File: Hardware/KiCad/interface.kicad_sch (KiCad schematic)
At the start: 26 parts, among them J6 UART, J7 OLED, SW10 SW_Push_45deg, SW11 SW_Push_45deg, SW12 SW_Push_45deg, SW13 SW_Push_45deg, SW14 SW_Push_45deg, SW15 SW_Push_45deg, SW16 SW_Push_45deg, SW17 SW_Push_45deg, SW2 SW_Push_45deg, SW3 SW_Push_45deg, SW4 SW_Push_45deg, SW5 SW_Push_45deg, SW6 SW_Push_45deg, SW7 SW_Push_45deg, SW8 SW_Push_45deg, SW9 SW_Push_45deg

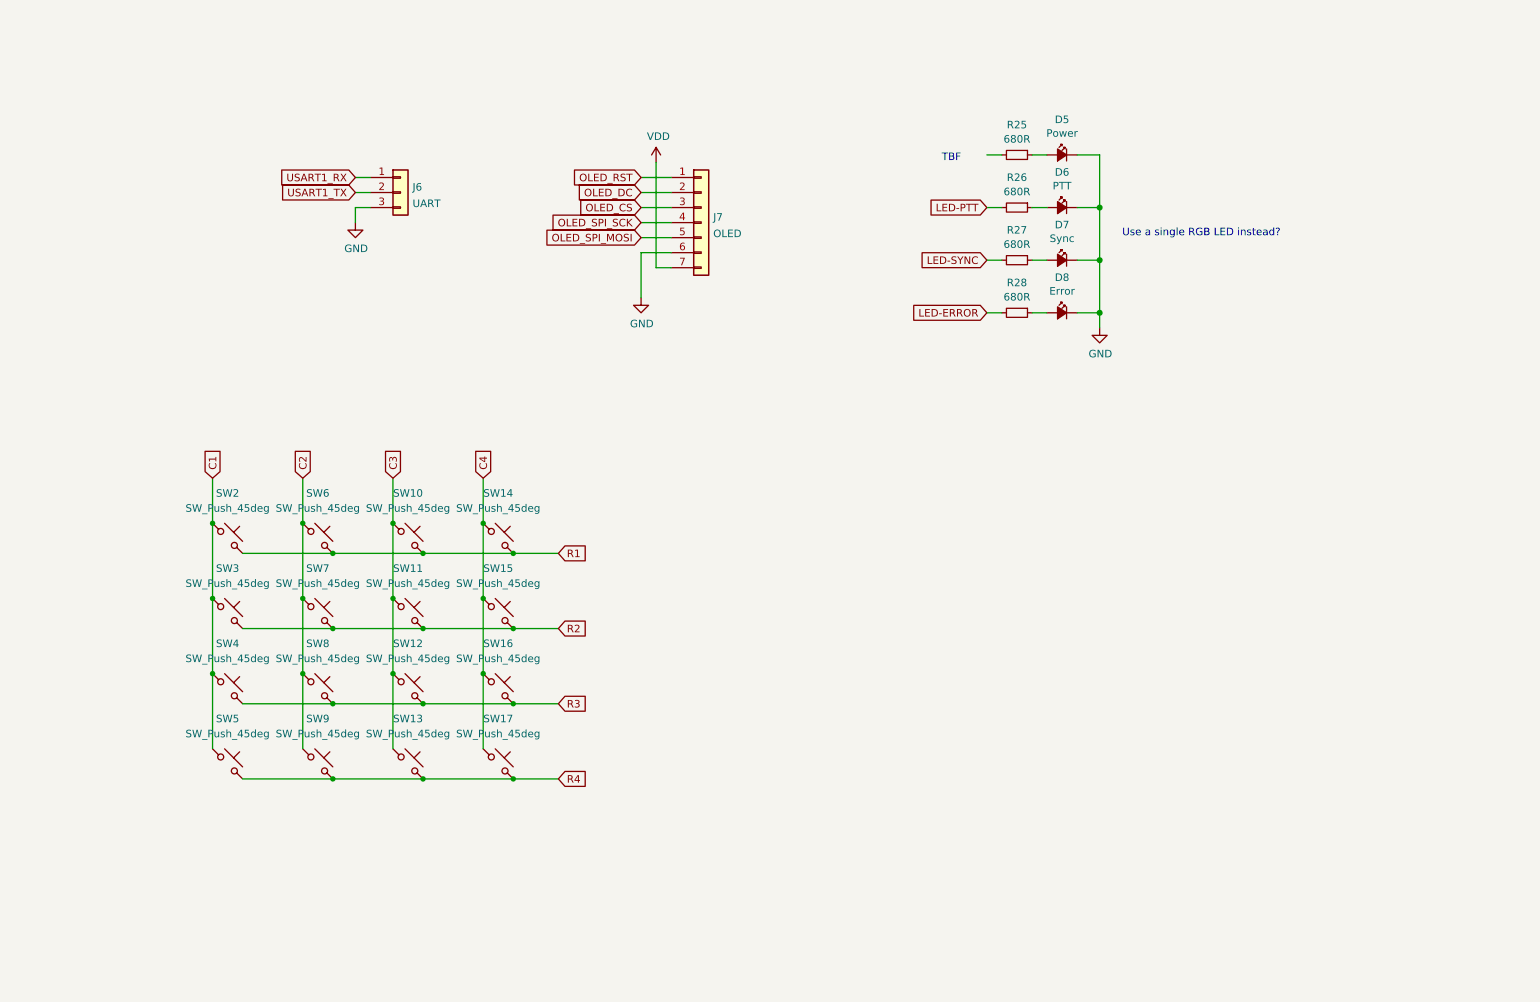
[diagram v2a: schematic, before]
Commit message: Connected SD card to the micro
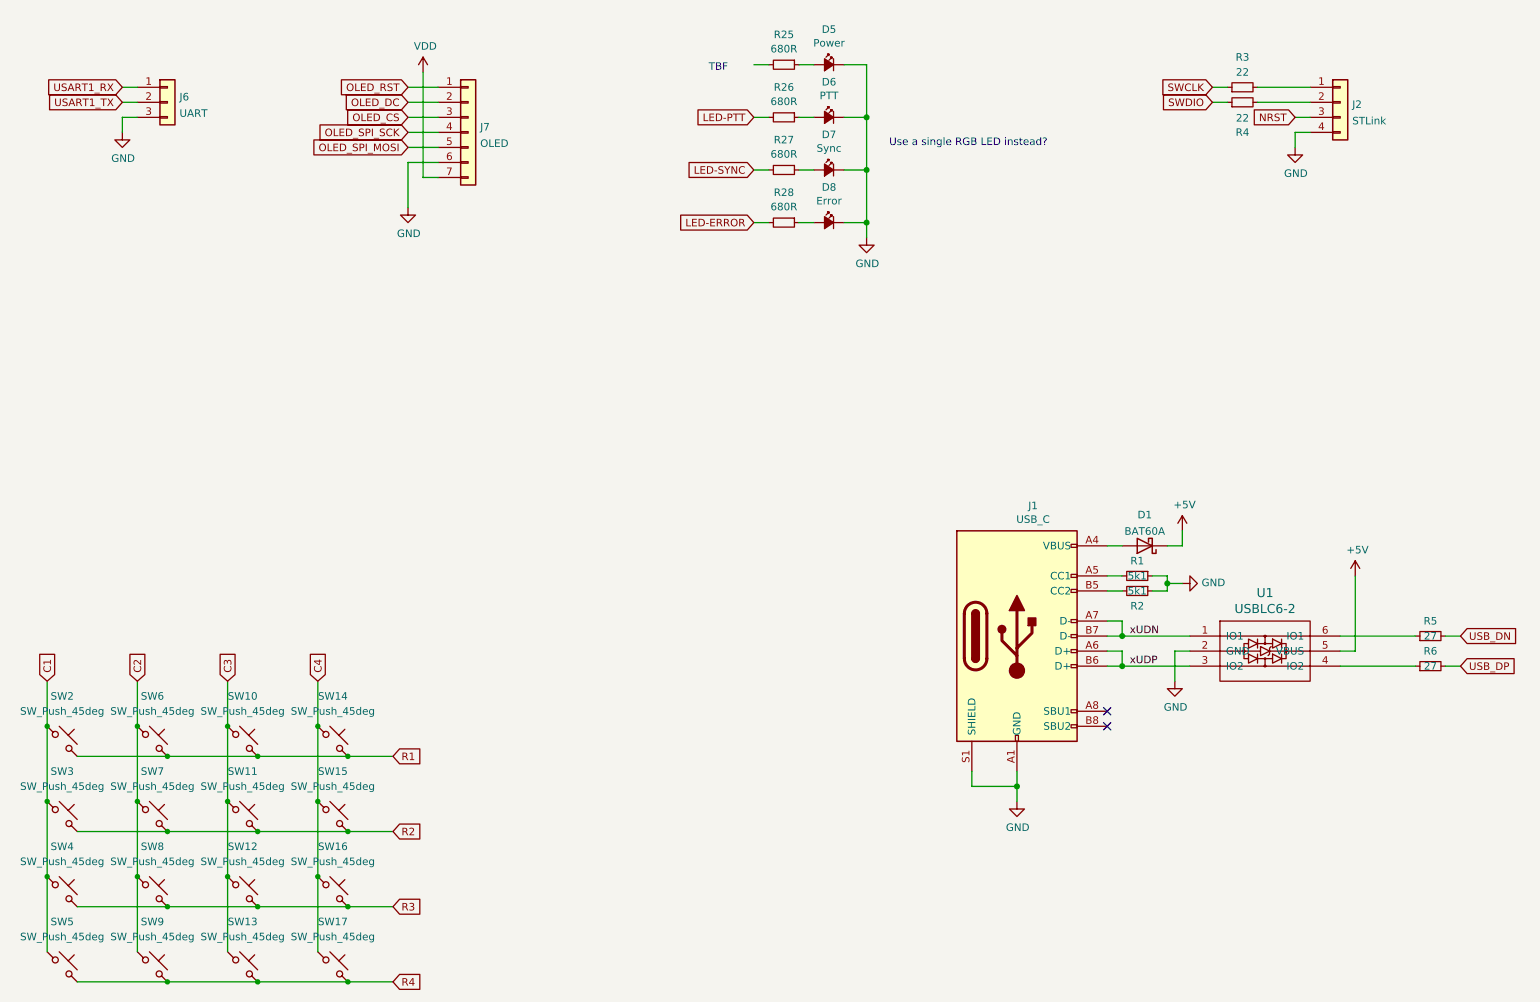
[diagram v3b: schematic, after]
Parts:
- added D1: BAT60A, Diode_SMD:D_SOD-323, symbol Diode:BAT60A
- added J1: USB_C, pkl_connectors:USB_C_Receptacle_HRO_TYPE-C-31-M-12, symbol Connector:USB_C_Receptacle_USB2.0
- added J2: STLink, Connector_PinHeader_2.54mm:PinHeader_1x04_P2.54mm_Vertical, symbol Connector_Generic:Conn_01x04
- added R1, R2: 5k1, Resistor_SMD:R_0402_1005Metric, symbol pkl_device:pkl_R_Small
- added R3, R4: 22, Resistor_SMD:R_0402_1005Metric, symbol pkl_device:pkl_R_Small
- added R5, R6: 27, Resistor_SMD:R_0402_1005Metric, symbol pkl_device:pkl_R_Small
- added U1: USBLC6-2, pkl_housings_sot:SOT-23-6, symbol pkl_misc:USBLC6-2
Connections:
- net GND: now also J1.A1 (GND), J1.A12 (GND), J1.B1 (GND), J1.B12 (GND), J1.S1 (SHIELD), J2.4 (Pin_4), R1.1, R2.1, U1.2 (GND)
- new net: R6.1, U1.4 (IO2)
- new net: R5.1, U1.6 (IO1)
- new net: J2.1 (Pin_1), R3.2
- new net: J2.2 (Pin_2), R4.2
- new net: D1.2 (A), J1.A4 (VBUS), J1.A9 (VBUS), J1.B4 (VBUS), J1.B9 (VBUS)
- new net: J1.A5 (CC1), R1.2
- new net: J1.B5 (CC2), R2.2
- new net +5V: D1.1 (K), U1.5 (VBUS)
- new net NRST: J2.3 (Pin_3)
- new net SWCLK: R3.1
- new net SWDIO: R4.1
- new net USB_DN: R5.2
- new net USB_DP: R6.2
- new net xUDN: J1.A7 (D-), J1.B7 (D-), U1.1 (IO1)
- new net xUDP: J1.A6 (D+), J1.B6 (D+), U1.3 (IO2)
- no-connect marks 0 -> 2
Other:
- moved on the sheet: D5, D6, D7, D8, J6, J7, R25, R26, R27, R28, SW10, SW11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

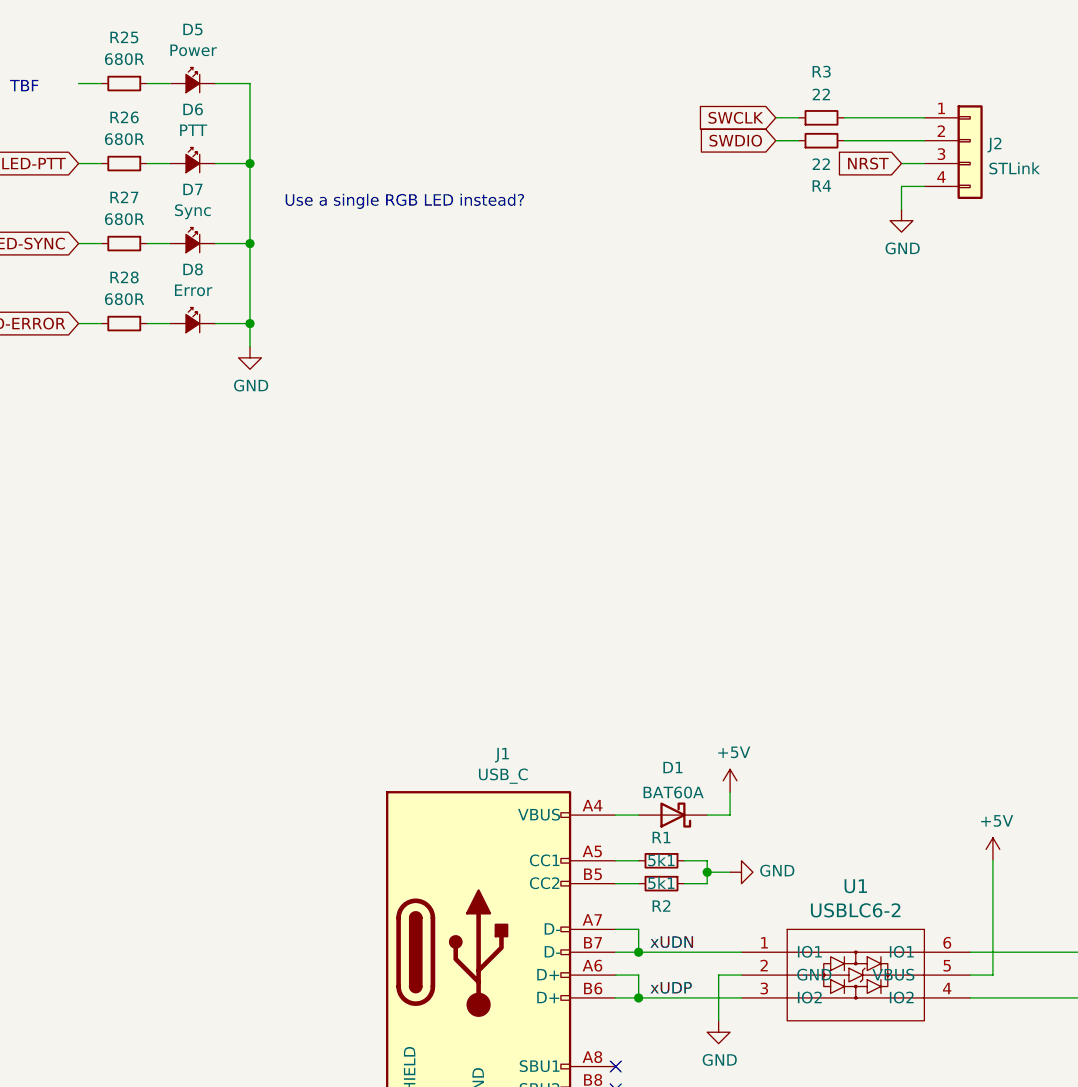
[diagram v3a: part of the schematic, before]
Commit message: adjust footprints
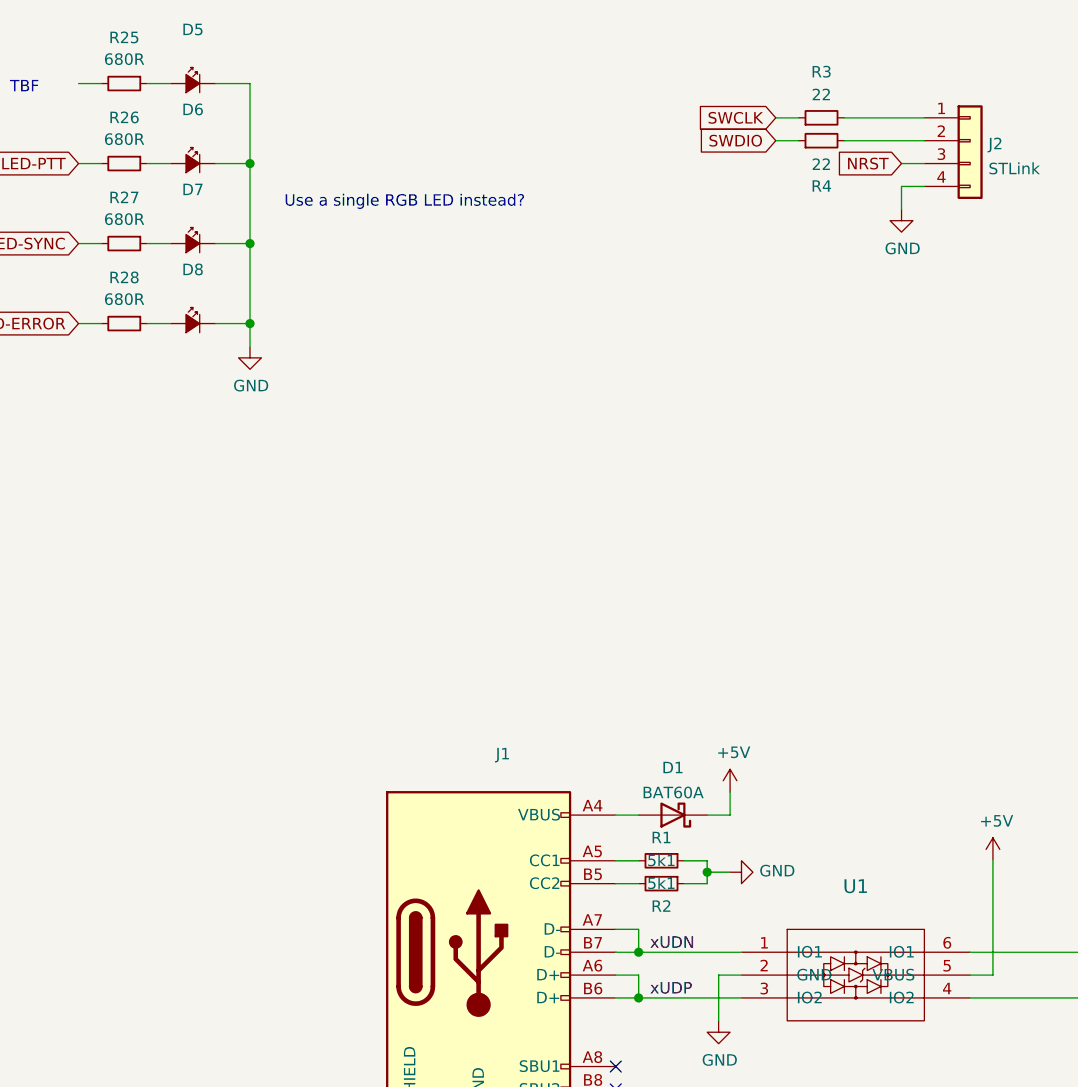
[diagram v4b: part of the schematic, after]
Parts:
- D5: value Power -> (none); footprint pkl_dipol:D_0603 -> (none)
- D6: value PTT -> (none); footprint pkl_dipol:D_0603 -> (none)
- D7: value Sync -> (none); footprint pkl_dipol:D_0603 -> (none)
- D8: value Error -> (none); footprint pkl_dipol:D_0603 -> (none)
- J1: value USB_C -> (none); footprint pkl_connectors:USB_C_Receptacle_HRO_TYPE-C-31-M-12 -> (none)
- U1: value USBLC6-2 -> (none); footprint pkl_housings_sot:SOT-23-6 -> (none)
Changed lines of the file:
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@@
       (effects (font (size 1.524 1.524)))
     )
-    (property "Value" "USBLC6-2" (id 1) (at 233.68 123.6726 0)
-      (effects (font (size 1.524 1.524)))
-    )
-    (property "Footprint" "pkl_housings_sot:SOT-23-6" (id 2) (at 233.68 130.81 0)
+    (property "Value" "" (id 1) (at 233.68 123.6726 0)
+      (effects (font (size 1.524 1.524)))
+    )
+    (property "Footprint" "" (id 2) (at 233.68 130.81 0)
       (effects (font (size 1.524 1.524)) hide)
     )
@@
     (in_bom yes) (on_board yes)
     (property "Reference" "D8" (id 0) (at 160.02 52.451 0))
-    (property "Value" "Error" (id 1) (at 160.02 54.7624 0))
-    (property "Footprint" "pkl_dipol:D_0603" (id 2) (at 160.02 58.42 90)
+    (property "Value" "" (id 1) (at 160.02 54.7624 0))
+    (property "Footprint" "" (id 2) (at 160.02 58.42 90)
       (effects (font (size 1.524 1.524)) hide)
     )
@@
     (in_bom yes) (on_board yes)
     (property "Reference" "D6" (id 0) (at 160.02 34.671 0))
-    (property "Value" "PTT" (id 1) (at 160.02 36.9824 0))
-    (property "Footprint" "pkl_dipol:D_0603" (id 2) (at 160.02 40.64 90)
+    (property "Value" "" (id 1) (at 160.02 36.9824 0))
+    (property "Footprint" "" (id 2) (at 160.02 40.64 90)
       (effects (font (size 1.524 1.524)) hide)
     )
@@
     (in_bom yes) (on_board yes)
     (property "Reference" "D7" (id 0) (at 160.02 43.561 0))
-    (property "Value" "Sync" (id 1) (at 160.02 45.8724 0))
-    (property "Footprint" "pkl_dipol:D_0603" (id 2) (at 160.02 49.53 90)
+    (property "Value" "" (id 1) (at 160.02 45.8724 0))
+    (property "Footprint" "" (id 2) (at 160.02 49.53 90)
       (effects (font (size 1.524 1.524)) hide)
     )
@@
     (in_bom yes) (on_board yes)
     (property "Reference" "D5" (id 0) (at 160.02 25.781 0))
-    (property "Value" "Power" (id 1) (at 160.02 28.0924 0))
-    (property "Footprint" "pkl_dipol:D_0603" (id 2) (at 160.02 31.75 90)
+    (property "Value" "" (id 1) (at 160.02 28.0924 0))
+    (property "Footprint" "" (id 2) (at 160.02 31.75 90)
       (effects (font (size 1.524 1.524)) hide)
     )
@@
     (in_bom yes) (on_board yes)
     (property "Reference" "J1" (id 0) (at 194.4878 106.2482 0))
-    (property "Value" "USB_C" (id 1) (at 194.4878 108.5596 0))
-    (property "Footprint" "pkl_connectors:USB_C_Receptacle_HRO_TYPE-C-31-M-12" (id 2) (at 195.58 128.27 0)
-      (effects (font (size 1.27 1.27)) hide)
-    )
+    (property "Value" "" (id 1) (at 194.4878 108.5596 0))
+    (property "Footprint" "" (id 2) (at 195.58 128.27 0)
+      (effects (font (size 1.27 1.27)) hide)
+    )
